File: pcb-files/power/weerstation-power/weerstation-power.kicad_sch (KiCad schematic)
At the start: 38 parts, among them J1 analoog bord connector power, J10 5v_power, J11 3.3v_power, J12 servo_power, J2 digitaal bord connector power, J3 zonnepanelen_12.3v, J4 batterij_laden_12.3v, J5 batterij_load_12.3v, J6 batterij_12.3v, J7 power_monitor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

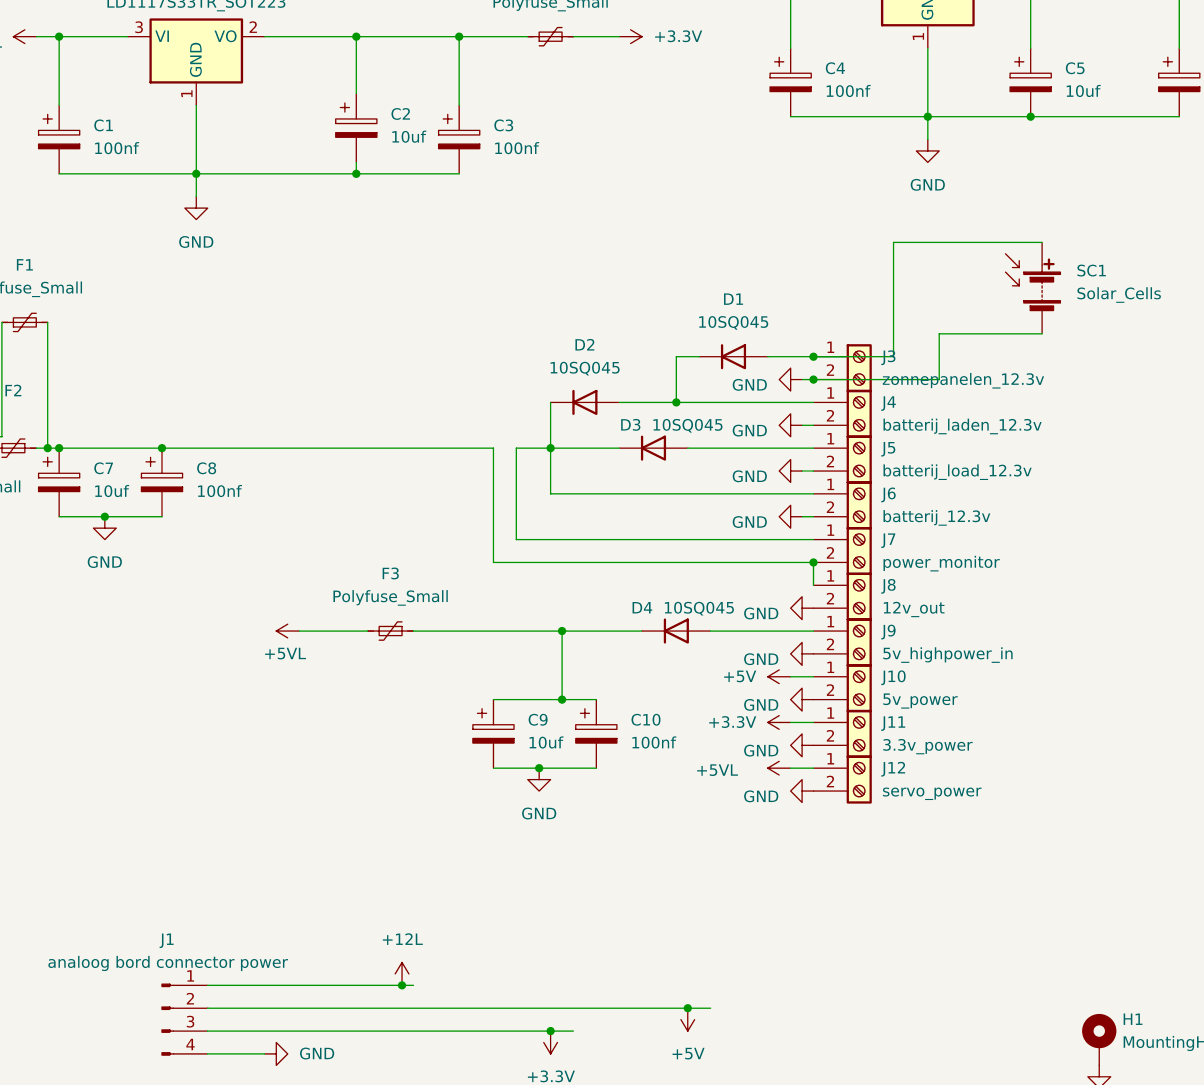
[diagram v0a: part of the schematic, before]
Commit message: update pcb files better layout and grounding inproved
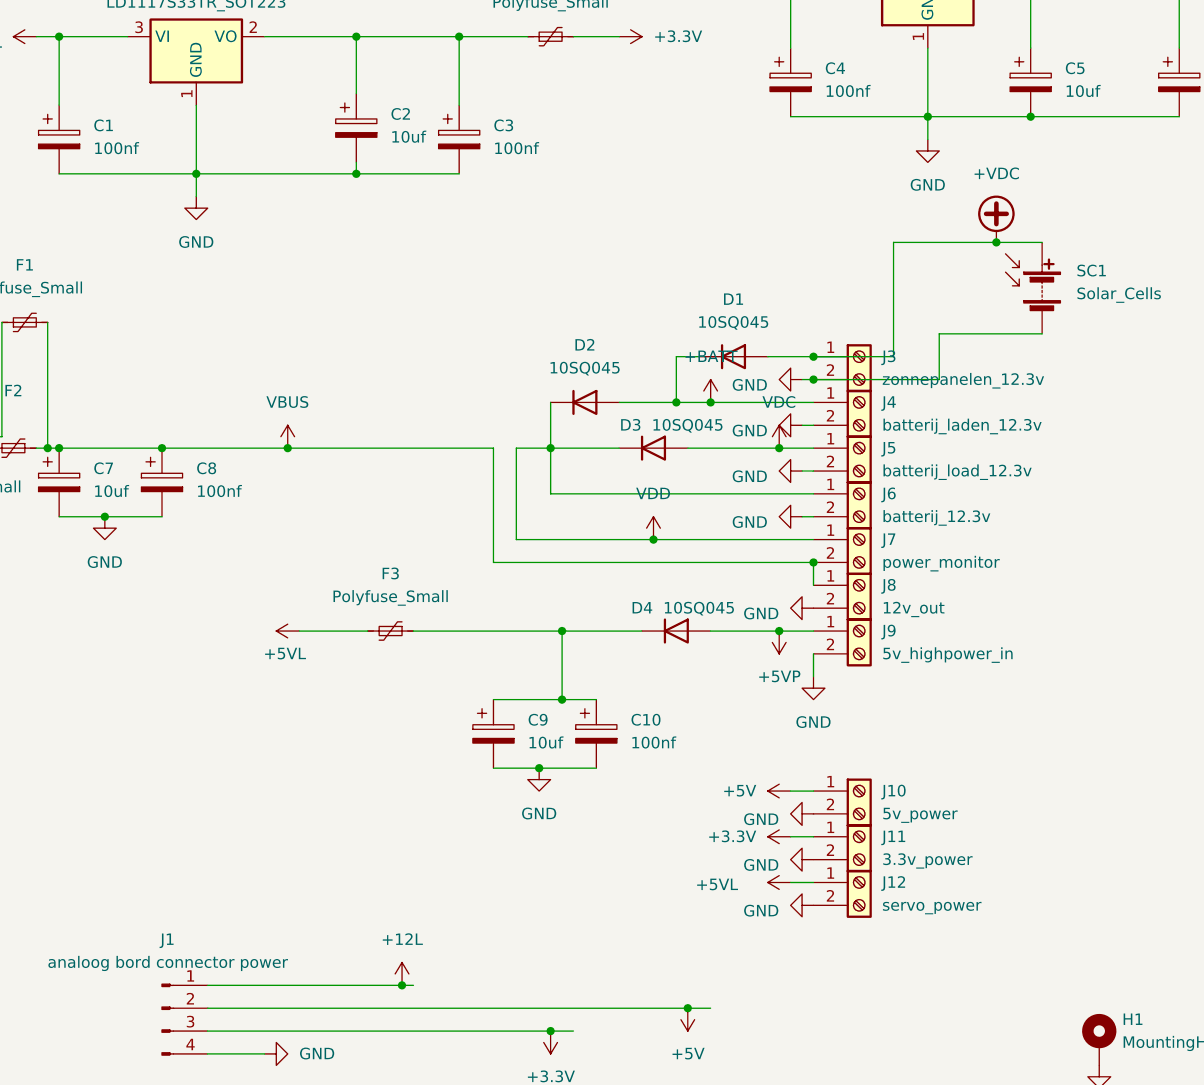
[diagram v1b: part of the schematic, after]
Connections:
- net VDD: now reaches D2.1 (K), D3.1 (K), J6.1 (Pin_1), J7.1 (Pin_1)
- net +BATT: now reaches D1.1 (K), D2.2 (A), J4.1 (Pin_1)
- net VBUS: now reaches C7.1, C8.1, F1.2, F2.1, J7.2 (Pin_2), J8.1 (Pin_1)
- net +VDC: now reaches D1.2 (A), J3.1 (Pin_1), SC1.1 (+)
- net VDC: now reaches D3.2 (A), J5.1 (Pin_1)
- net +5VP: now reaches D4.2 (A), J9.1 (Pin_1)
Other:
- moved on the sheet: J10, J11, J12
